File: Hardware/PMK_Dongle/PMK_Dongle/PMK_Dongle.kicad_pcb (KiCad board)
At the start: 4 copper layers, 10.4 x 20.1 mm, 31 parts, among them IC1 ESP32-S2FH4, J1 USB_A, U1 MIC5528-3.3YMT-T5, Y1 40MHz

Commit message: Layout is almost done
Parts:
- C11, C12, C13, C14, C15, C17, C18, C5, C6, C7, C8: moved to B.Cu
- D1: footprint Capacitor_SMD:C_0402_1005Metric -> LED_SMD:LED_0402_1005Metric
- L1: footprint Capacitor_SMD:C_0201_0603Metric -> Inductor_SMD:L_0201_0603Metric
- R1, R3: footprint Capacitor_SMD:C_0201_0603Metric -> Resistor_SMD:R_0201_0603Metric
- R2: footprint Capacitor_SMD:C_0402_1005Metric -> Resistor_SMD:R_0402_1005Metric
- R4: footprint Capacitor_SMD:C_0201_0603Metric -> Resistor_SMD:R_0402_1005Metric; moved to F.Cu
- moved C17 22.0 mm to (148.5, 38.2), turned to 90 degrees
- moved C6 19.8 mm to (153.7, 47.3), turned to -90 degrees
- moved C12 18.9 mm to (148.9, 45.0), turned to 135 degrees
- moved C13 18.8 mm to (150.1, 45.0), turned to 135 degrees
- moved C8 18.5 mm to (152.6, 47.3), turned to -90 degrees
- moved C11 16.6 mm to (148.9, 47.2), turned to -90 degrees
- moved C18 14.0 mm to (151.5, 35.8), turned to 90 degrees
- moved C15 10.9 mm to (156.8, 37.3), turned to -45 degrees
- moved C5 10.2 mm to (157.6, 43.8), turned to -90 degrees
- moved C14 9.21 mm to (155.6, 37.3), turned to -45 degrees
- moved C7 7.70 mm to (157.1, 45.3), turned to -45 degrees
- moved C16 4.74 mm to (153.6, 49.3)
- moved R4 4.65 mm to (153.6, 47.6)
- moved R1 4.33 mm to (155.8, 45.3), turned to 135 degrees
- moved R3 4.21 mm to (150.1, 37.0), turned to 0 degrees
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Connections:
- R2 pad 1: /IO15 -> /IO46
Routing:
- net +3V3: track 0.00 -> 15.6 mm
- net /VDD_SPI: track 0.00 -> 2.70 mm
- net /IO18: track 0.00 -> 1.40 mm
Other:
- board size 10.4 x 20.1 mm -> 10.4 x 18.3 mm

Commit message: Routing ongoing
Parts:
- moved C16 0.80 mm to (153.6, 50.1)
- moved D1 0.80 mm to (152.4, 50.1)
- moved C17 0.72 mm to (148.9, 38.8), turned to -135 degrees
- moved C7 0.65 mm to (156.6, 44.8)
- moved U1 0.58 mm to (155.4, 35.3)
- moved C5 0.54 mm to (157.4, 43.3), turned to -135 degrees
- moved R3 0.51 mm to (150.2, 37.5), turned to 45 degrees
- moved C6 0.20 mm to (153.5, 47.3)
- moved C8 0.10 mm to (152.5, 47.3)
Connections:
- S1 pad 3: (no net) -> /EN
- S2 pad 3: (no net) -> /IO0
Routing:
- net /EN: track 0.00 -> 9.02 mm, vias 0 -> 1
- net VBUS: track 0.00 -> 7.20 mm, vias 0 -> 1
- net /IO0: track 0.00 -> 5.94 mm, vias 0 -> 1
- net /IO46: track 0.00 -> 3.92 mm, vias 0 -> 1
- net Net-(ANT1-Pad1): track 0.00 -> 2.93 mm
- net /QUARTZ_1: track 0.00 -> 2.09 mm
- net /LNA_IN: track 0.00 -> 2.02 mm
- net Net-(D1-Pad2): track 0.00 -> 1.55 mm
- net GND: track 0.00 -> 1.42 mm, vias 0 -> 9
- net +3V3: track 15.6 -> 16.5 mm
- net /QUARTZ_2: track 0.00 -> 0.92 mm
- added copper zone on B.Cu, net GND
- added copper zone on F.Cu, net GND
- added copper zone on In1.Cu, net GND
- added copper zone on In2.Cu, net GND

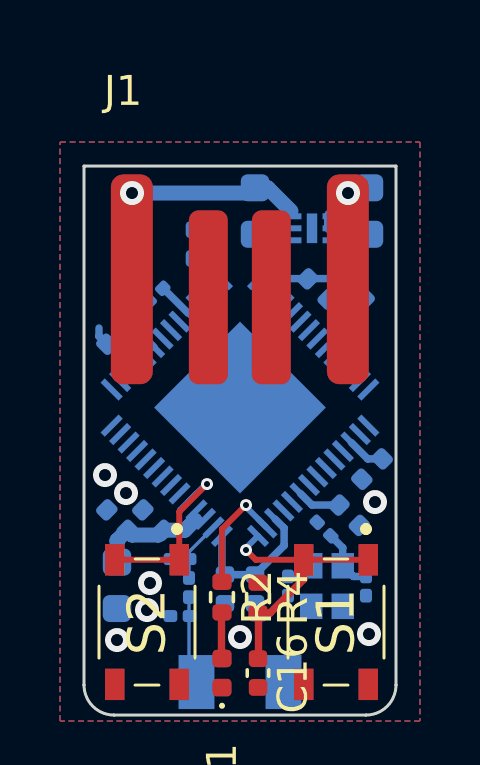
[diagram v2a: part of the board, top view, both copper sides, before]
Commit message: Updated routing to jlc specifications
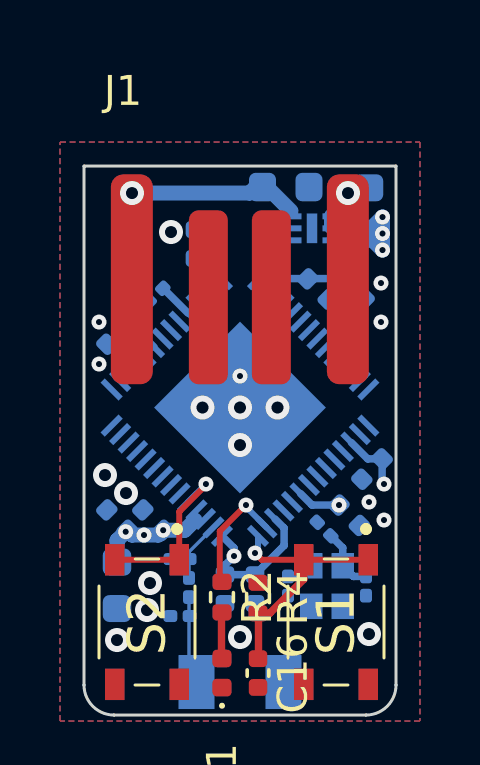
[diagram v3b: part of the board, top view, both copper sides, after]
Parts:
- moved C1 1.30 mm to (154.5, 33.9), turned to 0 degrees
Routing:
- net +3V3: track 16.5 -> 20.8 mm, vias 0 -> 9
- net GND: track 1.42 -> 0.77 mm, vias 9 -> 20
- added copper zone on In1.Cu, net +3V3

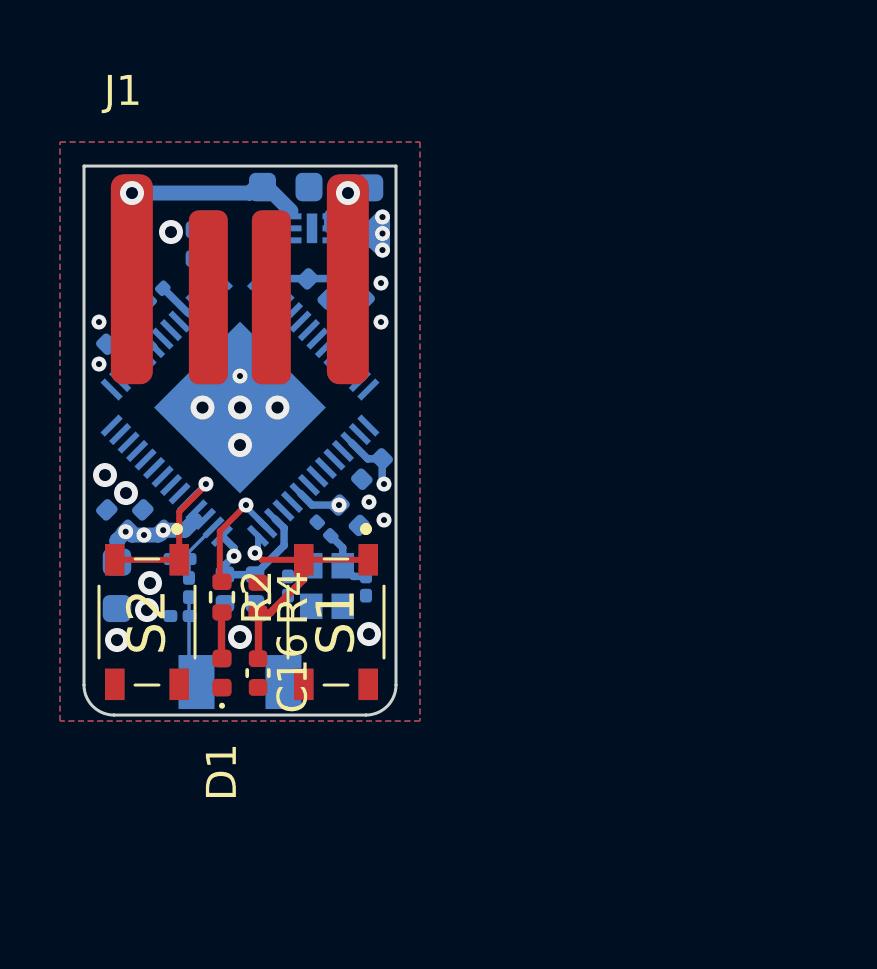
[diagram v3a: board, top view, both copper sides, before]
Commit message: Routing is almost done, just need to check quartz
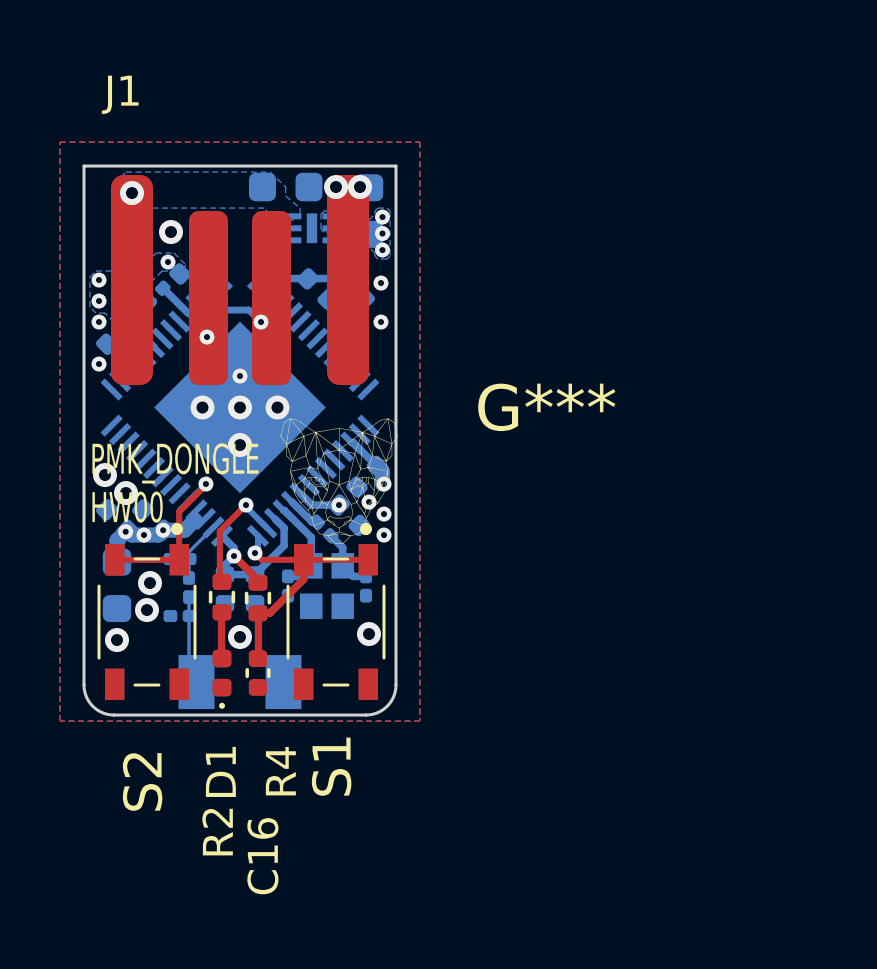
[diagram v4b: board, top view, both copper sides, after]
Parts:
- added G***: LOGO, Component_lib:puma_logo_4mm, F.Cu at (156.3, 43.7)
- moved C3 2.60 mm to (154.6, 47.2)
- moved C4 2.60 mm to (157.2, 47.2)
- moved C18 0.68 mm to (151.3, 36.5), turned to 45 degrees
- moved C5 0.31 mm to (157.2, 43.6)
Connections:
- IC1 pad 52: /QUARTZ_2 -> /QUARTZ_3
- IC1 pad 53: /QUARTZ_3 -> /QUARTZ_1
- R1 pad 1: /QUARTZ_1 -> /QUARTZ_2
- S1 pad 3: /EN -> (no net)
- S2 pad 3: /IO0 -> (no net)
- S2 pad 4: (no net) -> GND
- Y1 pad 1: /QUARTZ_1 -> /QUARTZ_2
- Y1 pad 4: /QUARTZ_2 -> /QUARTZ_1
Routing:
- net VBUS: track 7.20 -> 0.00 mm
- net +3V3: track 20.8 -> 16.1 mm, vias 9 -> 12
- net /D+: track 0.00 -> 2.22 mm, vias 0 -> 1
- net /D-: track 0.00 -> 1.22 mm, vias 0 -> 1
- net /QUARTZ_2: track 0.92 -> 2.09 mm
- net /QUARTZ_3: track 0.00 -> 1.12 mm
- net /QUARTZ_1: track 2.09 -> 3.17 mm
- net GND: track 0.77 -> 0.25 mm, vias 20 -> 22
- added copper zone on B.Cu, net +3V3
- added copper zone on B.Cu, net VBUS
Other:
- board text added: "PMK_DONGLE HW00"

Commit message: Routing is done
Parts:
- Y1: value 40MHz -> Crystal_GND24_Small; footprint Component_lib:NX2016SA32MEXS00ACS06465 -> Component_lib:Crystal_SMD_2016-4Pin_2.0x1.6mm
- moved R1 1.03 mm to (154.9, 45.8), turned to 90 degrees
- moved C3 0.92 mm to (155.1, 48.0), turned to -45 degrees
- moved C4 0.71 mm to (157.1, 47.9), turned to -135 degrees
- moved Y1 0.39 mm to (156.2, 46.9), turned to 45 degrees
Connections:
- IC1 pad 52: /QUARTZ_3 -> /QUARTZ_2
- IC1 pad 53: /QUARTZ_1 -> /QUARTZ_3
- R1 pad 1: /QUARTZ_2 -> /QUARTZ_1
- S2 pad 4: GND -> (no net)
- Y1 pad 1: /QUARTZ_2 -> /QUARTZ_1
- Y1 pad 3: GND -> /QUARTZ_2
- Y1 pad 4: /QUARTZ_1 -> GND
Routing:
- net /QUARTZ_2: track 2.09 -> 5.00 mm
- net /QUARTZ_1: track 3.17 -> 1.99 mm
